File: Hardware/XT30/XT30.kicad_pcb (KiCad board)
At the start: 2 copper layers, 30 x 14 mm, 3 parts, among them J1 XT30PW-F

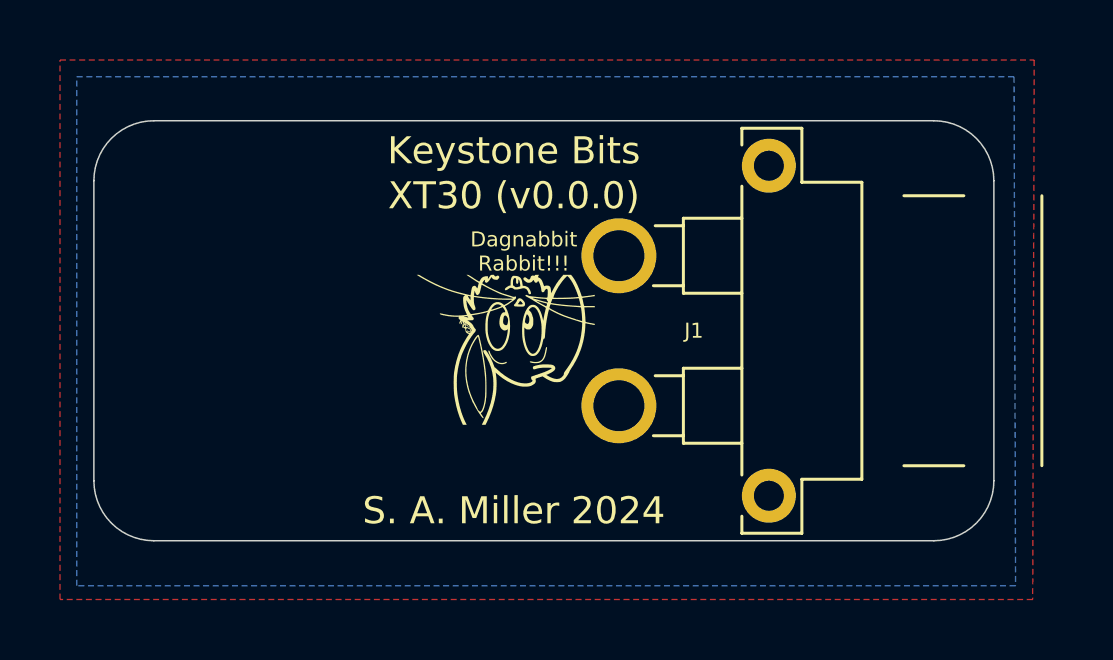
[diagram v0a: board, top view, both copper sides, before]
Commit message: Found the male XT30 & improved the XT30 board
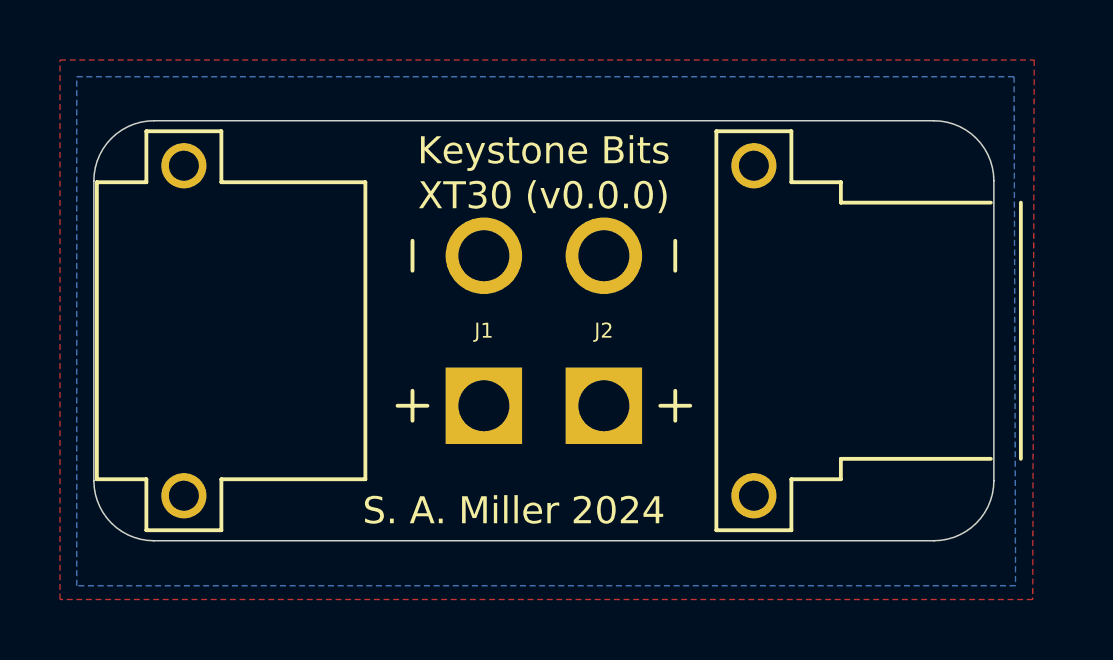
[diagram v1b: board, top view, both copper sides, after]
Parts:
- added J1: XT30PW-M, tinker:AMASS_XT30PW-M, F.Cu at (88.0, 100.0)
- J2: renamed from J1; footprint tinker:CONN-TH_XT30PW-F-1 -> tinker:AMASS_XT30PW-F
- REF**: moved to B.Cu
- moved REF** 11.0 mm to (110.0, 100.0), turned to 0 degrees
- moved G*** 9.00 mm to (90.0, 100.0)
- moved J2 2.00 mm to (107.0, 100.0), turned to -90 degrees

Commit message: SnapEDA responds to issue submissions blindingly fast!
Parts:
- added G***: LOGO, tinker:NerdMage, F.Cu at (90.0, 100.0)
- added REF**: DagNabbit, tinker:DagNabbit, F.Cu at (110.0, 100.0)

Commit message: ...
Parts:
- moved G*** 1.00 mm to (89.0, 100.0) (x2)
- moved J2 1.00 mm to (108.0, 100.0)
- moved REF** 1.00 mm to (111.0, 100.0) (x2)
